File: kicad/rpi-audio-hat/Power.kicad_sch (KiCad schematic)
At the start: 24 parts, among them U5 TPS563203, U7 TPS563203, U8 TLV76150DCYR, U9 LP2985-3.3

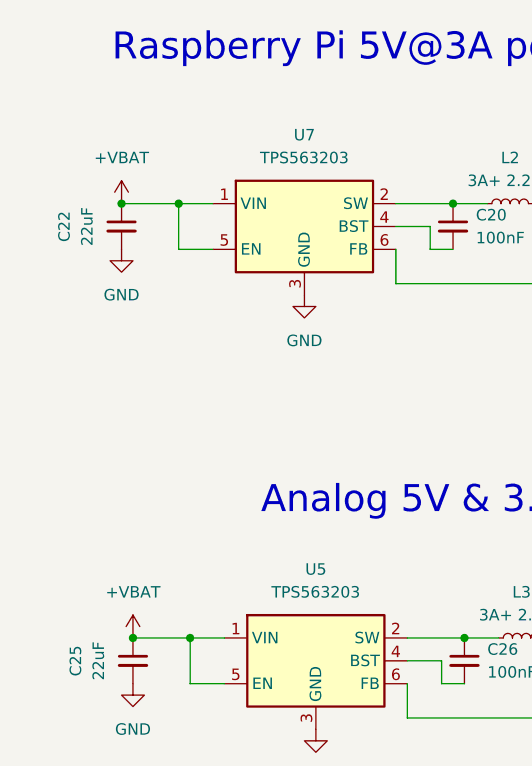
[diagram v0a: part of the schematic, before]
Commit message: Fix power switch & symbol update
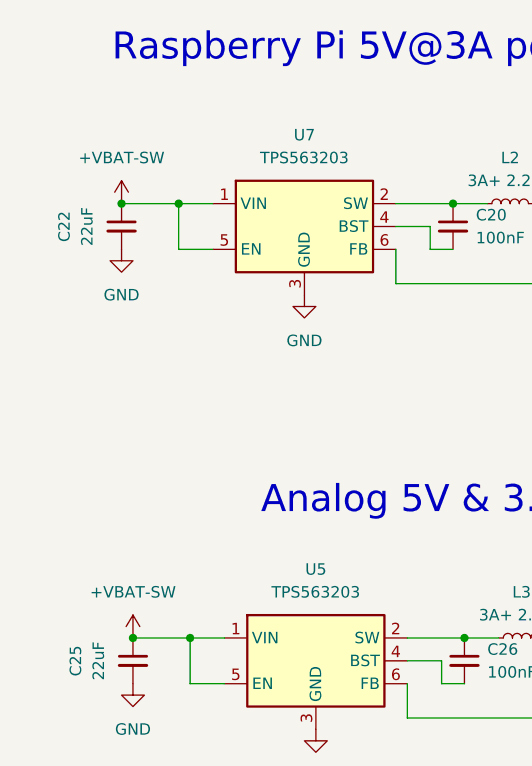
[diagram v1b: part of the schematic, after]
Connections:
- net +VBAT renamed +VBAT-SW
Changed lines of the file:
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@@
 	)
 	(junction
-		(at 52.07 50.8)
+		(at 110.49 50.8)
 		(diameter 0)
 		(color 0 0 0 0)
 	)
 	(junction
-		(at 110.49 50.8)
+		(at 190.5 99.06)
 		(diameter 0)
 		(color 0 0 0 0)
 	)
 	(junction
-		(at 190.5 99.06)
+		(at 53.34 99.06)
 		(diameter 0)
 		(color 0 0 0 0)
@@
 	)
 	(junction
-		(at 213.36 99.06)
+		(at 52.07 50.8)
 		(diameter 0)
 		(color 0 0 0 0)
 	)
 	(junction
-		(at 137.16 99.06)
+		(at 213.36 99.06)
 		(diameter 0)
 		(color 0 0 0 0)
 	)
 	(junction
-		(at 107.95 99.06)
+		(at 137.16 99.06)
 		(diameter 0)
 		(color 0 0 0 0)
 	)
 	(junction
-		(at 53.34 99.06)
+		(at 107.95 99.06)
 		(diameter 0)
 		(color 0 0 0 0)
@@
 	(symbol
 		(lib_id "power:+5V")
+		(at 53.34 99.06 0)
+		(unit 1)
+		(exclude_from_sim no)
+		(in_bom yes)
+		(on_board yes)
+		(dnp no)
+		(fields_autoplaced yes)
+		(property "Reference" "#PWR039"
+			(at 53.34 102.87 0)
+			(effects
+				(font
+					(size 1.27 1.27)
+				)
+				(hide yes)
+			)
+		)
+		(property "Value" "+VBAT-SW"
+			(at 53.34 93.98 0)
+			(effects
+				(font
+					(size 1.27 1.27)
+				)
+			)
+		)
+		(property "Footprint" ""
+			(at 53.34 99.06 0)
+			(effects
+				(font
+					(size 1.27 1.27)
+				)
+				(hide yes)
+			)
+		)
+		(property "Datasheet" ""
+			(at 53.34 99.06 0)
+			(effects
+				(font
+					(size 1.27 1.27)
+				)
+				(hide yes)
+			)
+		)
+		(property "Description" ""
+			(at 53.34 99.06 0)
+			(effects
+				(font
+					(size 1.27 1.27)
+				)
+				(hide yes)
+			)
+		)
+		(pin "1"
+		)
+		(instances
+			(project "rpi-audio-hat"
+				(path "/25d551e4-1e32-4b11-b540-b33b7fa395f8/d0ac3f21-db50-4e7b-8b35-74198b6a5fbf"
+					(reference "#PWR039")
+					(unit 1)
+				)
+			)
+		)
+	)
+	(symbol
+		(lib_id "power:+5V")
 		(at 137.16 97.79 0)
 		(unit 1)
@@
 	)
 	(symbol
-		(lib_id "power:+5V")
-		(at 52.07 50.8 0)
-		(unit 1)
-		(exclude_from_sim no)
-		(in_bom yes)
-		(on_board yes)
-		(dnp no)
-		(fields_autoplaced yes)
-		(property "Reference" "#PWR039"
-			(at 52.07 54.61 0)
-			(effects
-				(font
-					(size 1.27 1.27)
-				)
-				(hide yes)
-			)
-		)
-		(property "Value" "+VBAT"
-			(at 52.07 45.72 0)
-			(effects
-				(font
-					(size 1.27 1.27)
-				)
-			)
-		)
-		(property "Footprint" ""
-			(at 52.07 50.8 0)
-			(effects
-				(font
-					(size 1.27 1.27)
-				)
-				(hide yes)
-			)
-		)
-		(property "Datasheet" ""
-			(at 52.07 50.8 0)
-			(effects
-				(font
-					(size 1.27 1.27)
-				)
-				(hide yes)
-			)
-		)
-		(property "Description" ""
-			(at 52.07 50.8 0)
-			(effects
-				(font
-					(size 1.27 1.27)
-				)
-				(hide yes)
-			)
-		)
-		(pin "1"
-		)
-		(instances
-			(project "rpi-audio-hat"
-				(path "/25d551e4-1e32-4b11-b540-b33b7fa395f8/d0ac3f21-db50-4e7b-8b35-74198b6a5fbf"
-					(reference "#PWR039")
-					(unit 1)
-				)
-			)
-		)
-	)
-	(symbol
 		(lib_id "Device:C_Small")
 		(at 190.5 101.6 0)
@@
 	)
 	(symbol
+		(lib_id "power:+5V")
+		(at 52.07 50.8 0)
+		(unit 1)
+		(exclude_from_sim no)
+		(in_bom yes)
+		(on_board yes)
+		(dnp no)
+		(fields_autoplaced yes)
+		(property "Reference" "#PWR063"
+			(at 52.07 54.61 0)
+			(effects
+				(font
+					(size 1.27 1.27)
+				)
+				(hide yes)
+			)
+		)
+		(property "Value" "+VBAT-SW"
+			(at 52.07 45.72 0)
+			(effects
+				(font
+					(size 1.27 1.27)
+				)
+			)
+		)
+		(property "Footprint" ""
+			(at 52.07 50.8 0)
+			(effects
+				(font
+					(size 1.27 1.27)
+				)
+				(hide yes)
+			)
+		)
+		(property "Datasheet" ""
+			(at 52.07 50.8 0)
+			(effects
+				(font
+					(size 1.27 1.27)
+				)
+				(hide yes)
+			)
+		)
+		(property "Description" ""
+			(at 52.07 50.8 0)
+			(effects
+				(font
+					(size 1.27 1.27)
+				)
+				(hide yes)
+			)
+		)
+		(pin "1"
+		)
+		(instances
+			(project "rpi-audio-hat"
+				(path "/25d551e4-1e32-4b11-b540-b33b7fa395f8/d0ac3f21-db50-4e7b-8b35-74198b6a5fbf"
+					(reference "#PWR063")
+					(unit 1)
+				)
+			)
+		)
+	)
+	(symbol
 		(lib_id "Device:L_Small")
 		(at 95.25 50.8 90)
@@
 					(unit 1)
 				)
-			)
-		)
-	)
-	(symbol
-		(lib_id "power:+5V")
-		(at 53.34 99.06 0)
-		(unit 1)
-		(exclude_from_sim no)
-		(in_bom yes)
-		(on_board yes)
-		(dnp no)
-		(fields_autoplaced yes)
-		(property "Reference" "#PWR042"
-			(at 53.34 102.87 0)
-			(effects
-				(font
-					(size 1.27 1.27)
-				)
-				(hide yes)
-			)
-		)
-		(property "Value" "+VBAT"
-			(at 53.34 93.98 0)
-			(effects
-				(font
-					(size 1.27 1.27)
-				)
-			)
-		)
-		(property "Footprint" ""
-			(at 53.34 99.06 0)
-			(effects
-				(font
-					(size 1.27 1.27)
-				)
-				(hide yes)
-			)
-		)
-		(property "Datasheet" ""
-			(at 53.34 99.06 0)
-			(effects
-				(font
-					(size 1.27 1.27)
-				)
-				(hide yes)
-			)
-		)
-		(property "Description" ""
-			(at 53.34 99.06 0)
-			(effects
-				(font
-					(size 1.27 1.27)
-				)
-				(hide yes)
-			)
-		)
-		(pin "1"
-		)
-		(instances
-			(project "rpi-audio-hat"
-				(path "/25d551e4-1e32-4b11-b540-b33b7fa395f8/d0ac3f21-db50-4e7b-8b35-74198b6a5fbf"
-					(reference "#PWR042")
-					(unit 1)
-				)

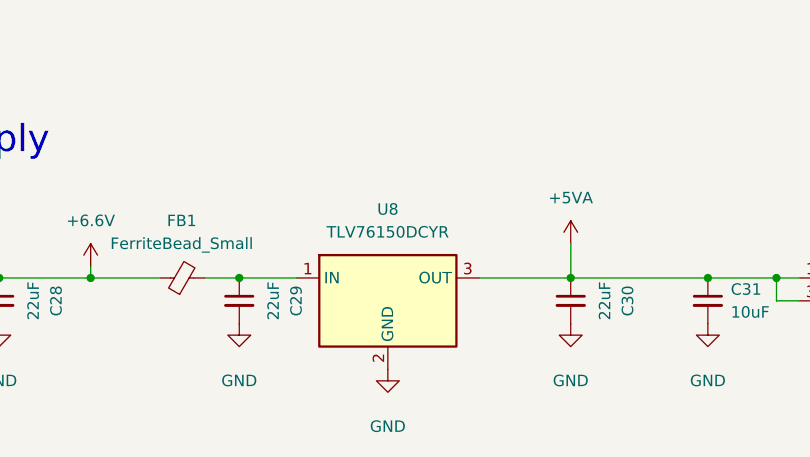
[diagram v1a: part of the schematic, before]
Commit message: Fix TLV761
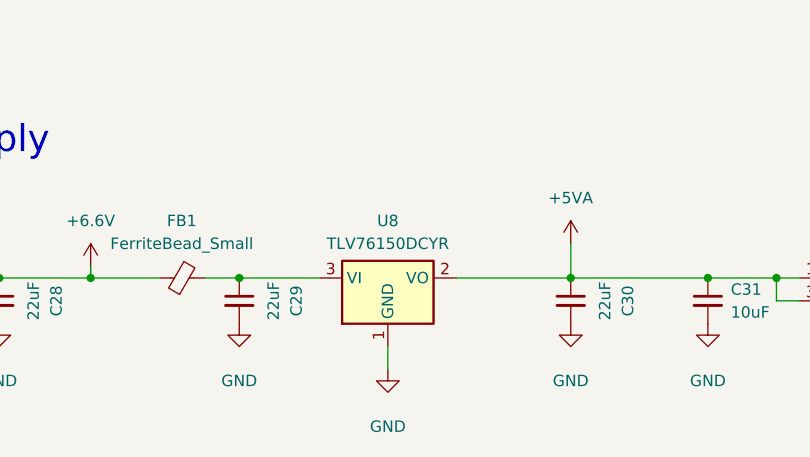
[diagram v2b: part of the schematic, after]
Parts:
- U8: symbol Regulator_Linear:LT1963AxST-3.3 -> Regulator_Linear:TLV76150DCY
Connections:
- net +5VA: now also U8.2 (VO); no longer U8.3 (OUT)
- net GND: now also U8.1 (GND); no longer U8.2 (GND)
- net at C29.1, FB1.2: now also U8.3 (VI); no longer U8.1 (IN)
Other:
- moved on the sheet: U8
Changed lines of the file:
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@@
 	(wire
 		(pts
-			(xy 180.34 99.06) (xy 190.5 99.06)
+			(xy 177.8 99.06) (xy 190.5 99.06)
 		)
 		(stroke
@@
 	(wire
 		(pts
+			(xy 170.18 106.68) (xy 170.18 109.22)
+		)
+		(stroke
+			(width 0)
+			(type default)
+		)
+	)
+	(wire
+		(pts
 			(xy 99.06 99.06) (xy 107.95 99.06)
 		)
@@
 	(wire
 		(pts
-			(xy 153.67 99.06) (xy 160.02 99.06)
+			(xy 153.67 99.06) (xy 162.56 99.06)
 		)
 		(stroke
@@
 	)
 	(symbol
-		(lib_id "Regulator_Linear:LT1963AxST-3.3")
-		(at 170.18 101.6 0)
+		(lib_id "Regulator_Linear:TLV76150DCY")
+		(at 170.18 99.06 0)
 		(unit 1)
 		(exclude_from_sim no)
@@
 		(fields_autoplaced yes)
 		(property "Reference" "U8"
-			(at 170.18 91.44 0)
+			(at 170.18 92.71 0)
 			(effects
 				(font
@@
 		)
 		(property "Value" "TLV76150DCYR"
-			(at 170.18 93.98 0)
+			(at 170.18 95.25 0)
 			(effects
 				(font
@@
 		)
 		(property "Footprint" "Package_TO_SOT_SMD:SOT-223-3_TabPin2"
+			(at 170.18 110.49 0)
+			(effects
+				(font
+					(size 1.27 1.27)
+				)
+				(hide yes)
+			)
+		)
+		(property "Datasheet" "https://www.ti.com/lit/ds/symlink/tlv761.pdf"
 			(at 170.18 113.03 0)
 			(effects
@@
 			)
 		)
-		(property "Datasheet" "https://www.analog.com/media/en/technical-documentation/data-sheets/1963aff.pdf"
-			(at 170.18 115.57 0)
-			(effects
-				(font
-					(size 1.27 1.27)
-				)
-				(hide yes)
-			)
-		)
-		(property "Description" "3.3V, 1.5A, Low Noise, Fast Transient Response LDO Regulator, SOT-223"
-			(at 170.18 101.6 0)
-			(effects
-				(font
+		(property "Description" "5.0V, 1A, Low Noise, High-PSRR LDO Regulator, 2.5V...16V input, SOT-223"
+			(at 170.18 99.06 0)
+			(effects
+				(font
